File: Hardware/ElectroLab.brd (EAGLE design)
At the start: 175 x 100 mm, 230 parts, among them IC1 LM2902DT, IC10 CD4511BNSR, IC11 PAM8403, IC13 ADXL337, IC14 MIC5205, IC2 LM2902DT, IC3 SN74LV08ADR, IC4 SN74LV32ADR, IC5 SN74LV04ADR, IC6 4027D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

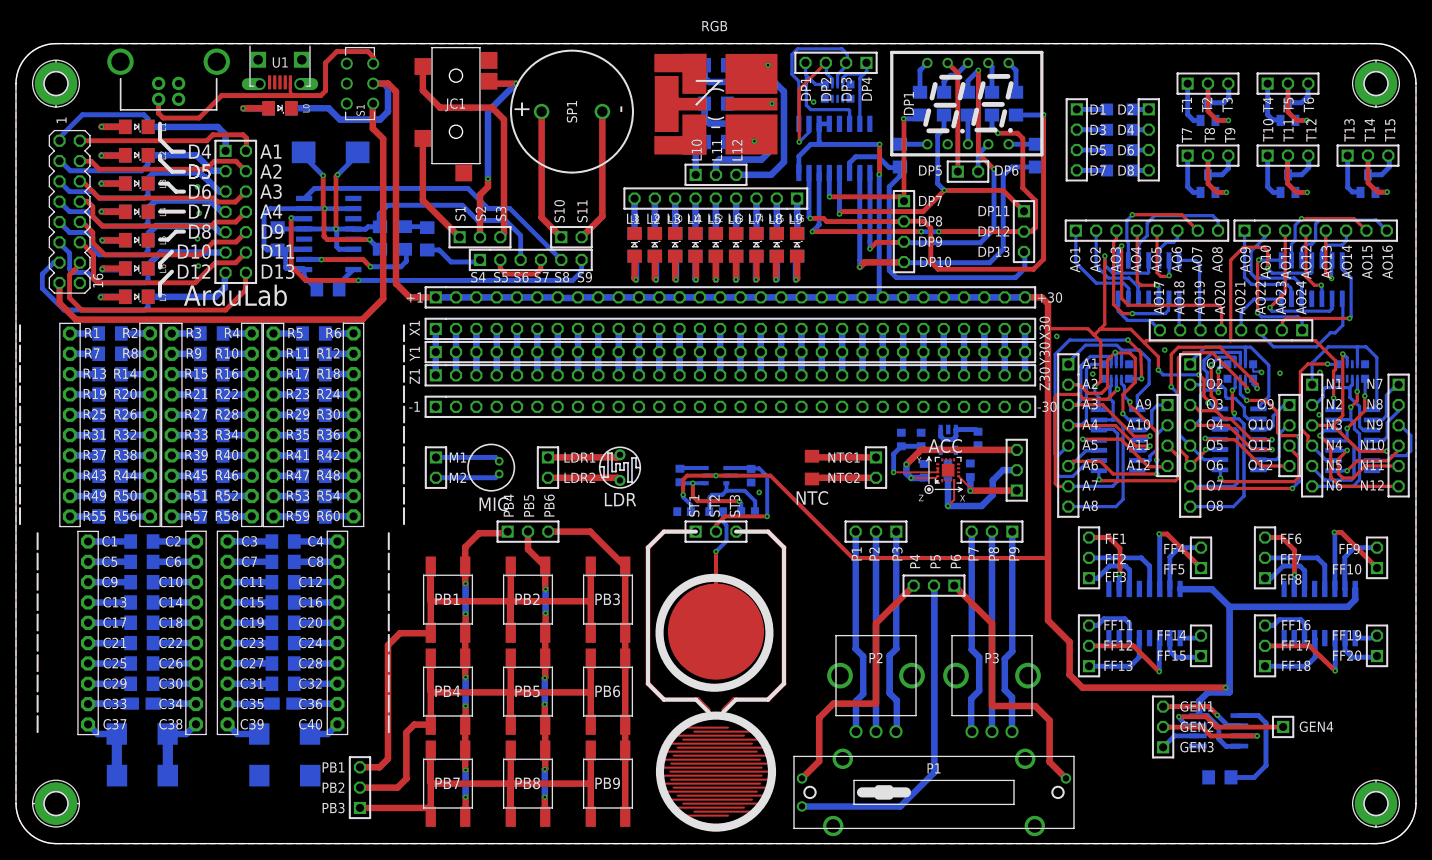
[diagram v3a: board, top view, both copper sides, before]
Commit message: Updated board layout and silkscreen
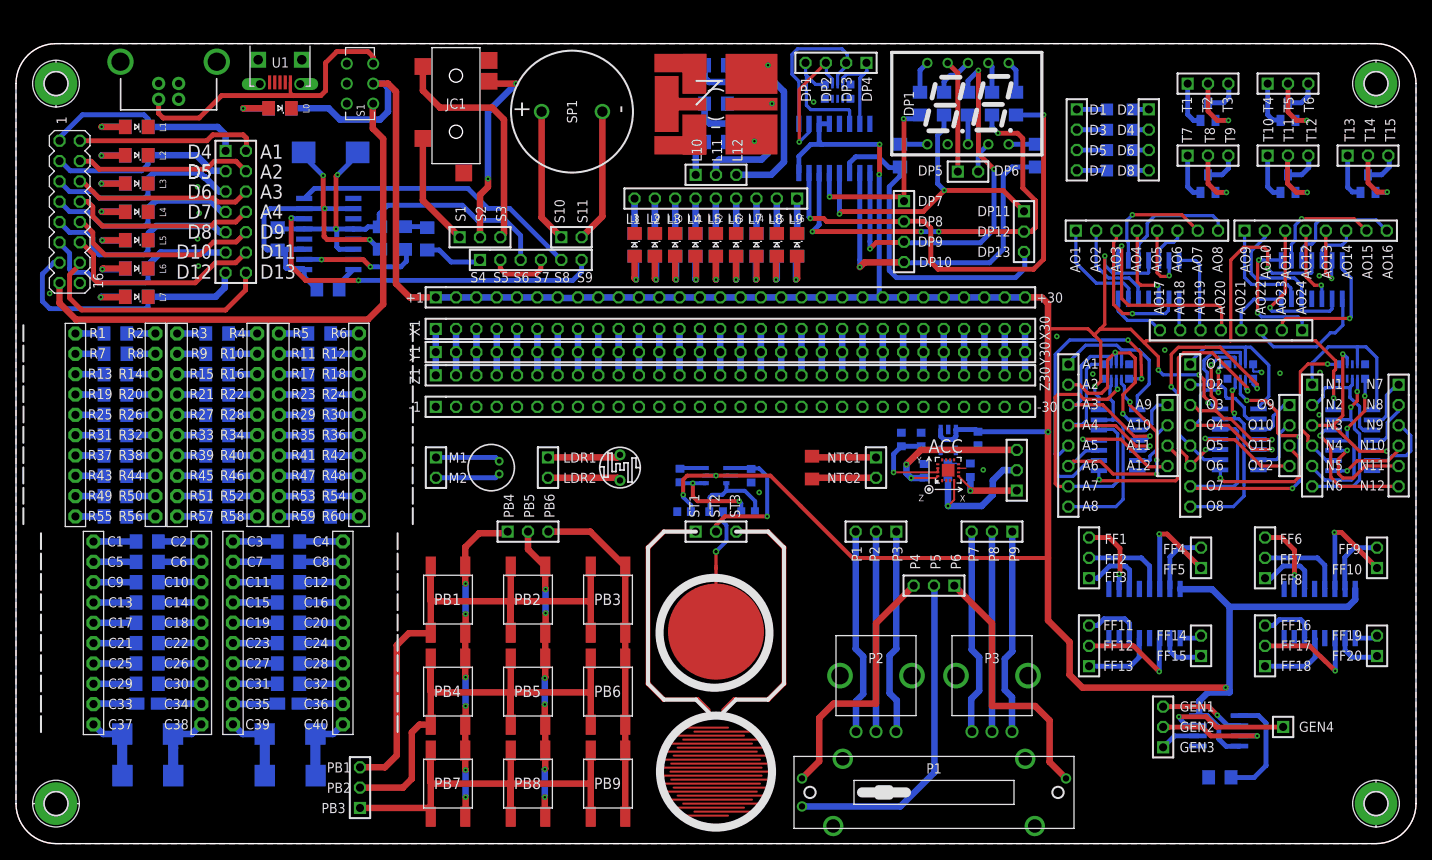
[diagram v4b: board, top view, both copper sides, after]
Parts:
- moved C1 0.68 mm to (34.1, 37.8)
- moved C11 0.68 mm to (34.1, 25.1)
- moved C13 0.68 mm to (34.1, 22.5)
- moved C15 0.68 mm to (34.1, 20.0)
- moved C17 0.68 mm to (34.1, 17.5)
- moved C3 0.68 mm to (34.1, 35.2)
- moved C35 0.68 mm to (34.3, 8.50)
- moved C5 0.68 mm to (34.1, 32.7)
- moved C7 0.68 mm to (34.1, 30.1)
- moved C9 0.68 mm to (34.1, 27.6)
- moved PH50 0.68 mm to (20.1, 52.3)
- moved PH51 0.68 mm to (30.1, 52.3)
- moved PH52 0.68 mm to (32.9, 52.3)
- moved PH53 0.68 mm to (42.9, 52.3)
- moved PH57 0.68 mm to (40.9, 26.3)
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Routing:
- net VCC: track 457.7 -> 466.5 mm, vias 12 -> 13
- net N$70: track 4.46 -> 9.67 mm
- net N$80: track 3.93 -> 9.14 mm
- net N$117: track 5.58 -> 8.17 mm
- net GND: track 64.3 -> 66.7 mm, vias 16 -> 19
- net SENSE: track 9.82 -> 7.72 mm, vias 1 -> 2
- net D12: track 32.2 -> 33.0 mm
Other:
- board text removed: "0000-0 0001-1 0010-2 0011-3 0100-4 0101-5 0110-6 0111-7 1000-8 1001-9"
- board text removed: "100"
- board text removed: "100K"
- board text removed: "100n"
- board text removed: "100p"
- board text removed: "100u"
- board text removed: "10K"
- board text removed: "10n"
- board text removed: "10p"
- board text removed: "10u"
- board text removed: "15K"
- board text removed: "1K"
- board text removed: "1m"
- board text removed: "1n"
- board text removed: "1u"
- board text removed: "4.7K"
- board text removed: "470"
- board text removed: "470K"
- board text removed: "47K"
- board text removed: "50n"
- board text removed: "AUX"
- board text removed: "ArduLab"
- board text removed: "Blue"
- board text removed: "DIS"
- board text removed: "Dig 1"
- board text removed: "Dig 2"
- board text removed: "Green"
- board text removed: "J"
- board text removed: "K"
- board text removed: "L"
- board text removed: "NPN"
- board text removed: "NTC"
- board text removed: "OUT"
- board text removed: "PNP"
- board text removed: "Power"
- board text removed: "Q"
- board text removed: "R"
- board text removed: "Red"
- board text removed: "THR"
- board text removed: "TRIG"
- board text removed: "USB"
- board text removed: "X"
- board text removed: "Y"
- board text removed: "Z"
